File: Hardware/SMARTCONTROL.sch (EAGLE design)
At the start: 36 parts, among them IC1 ESP12-SMT, J1 ESPFLASH-1X6-2.54-SOCKET, Q2 RJU003N03, Q3 RJU003N03, Q4 RJU003N03, Q5 RJU003N03

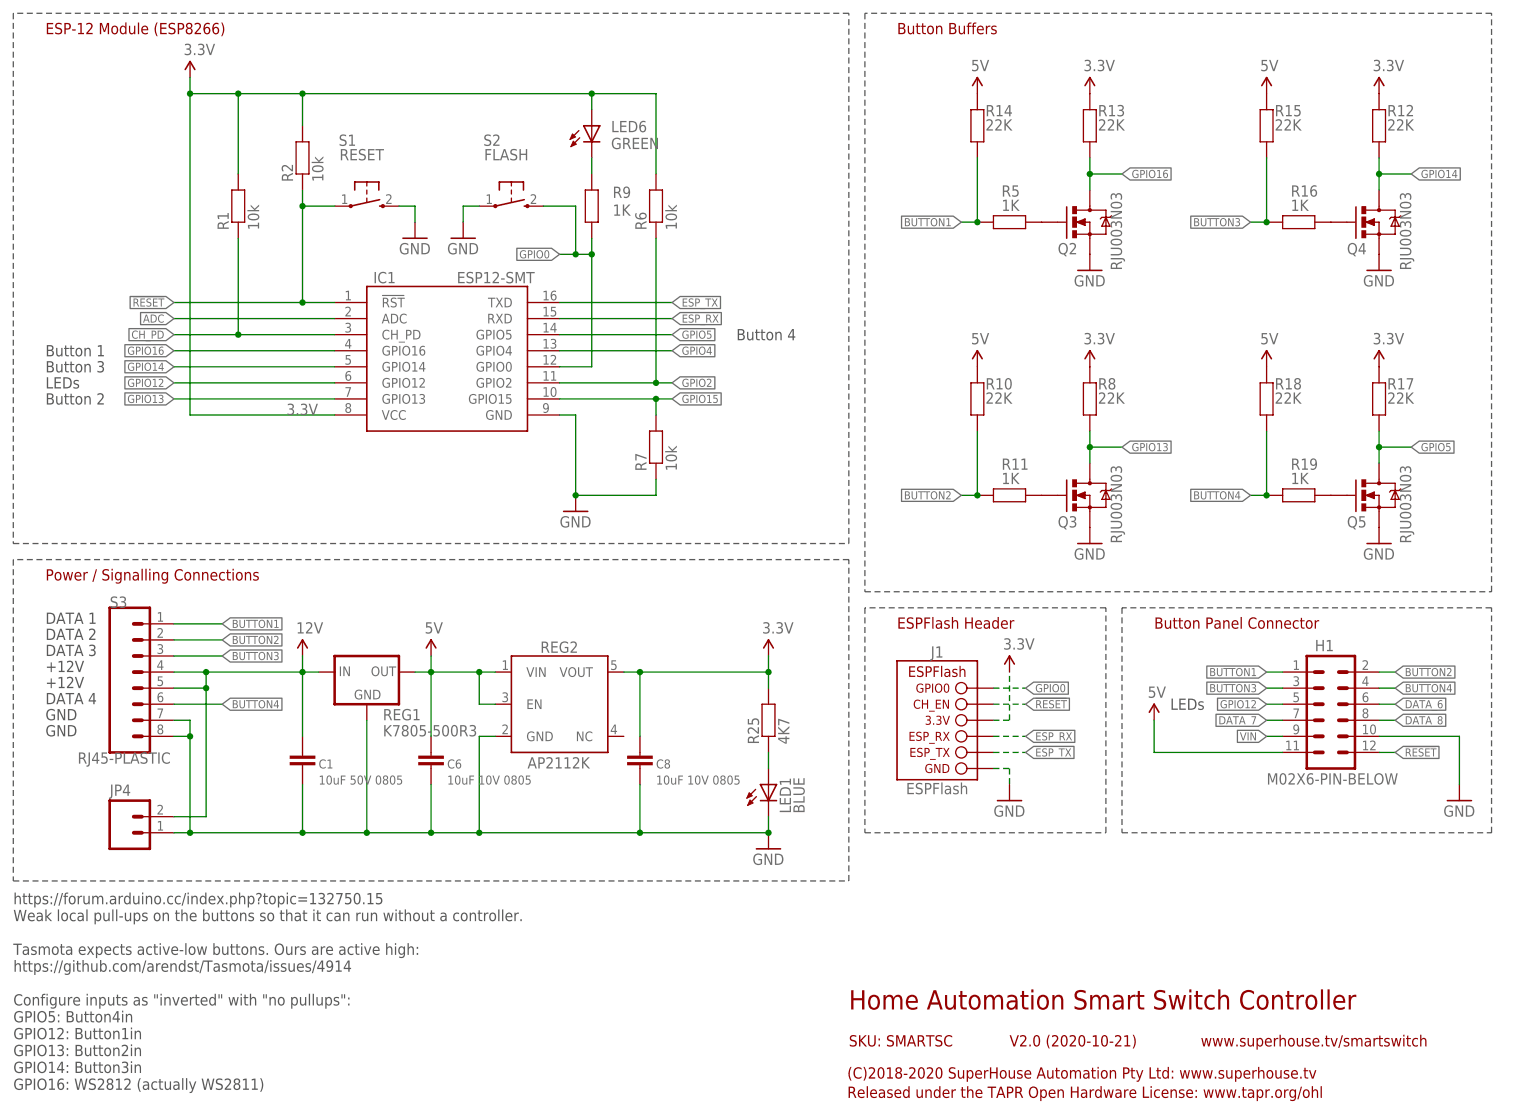
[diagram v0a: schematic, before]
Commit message: Converted switch isolation from FETs to diodes for v2.1 release.
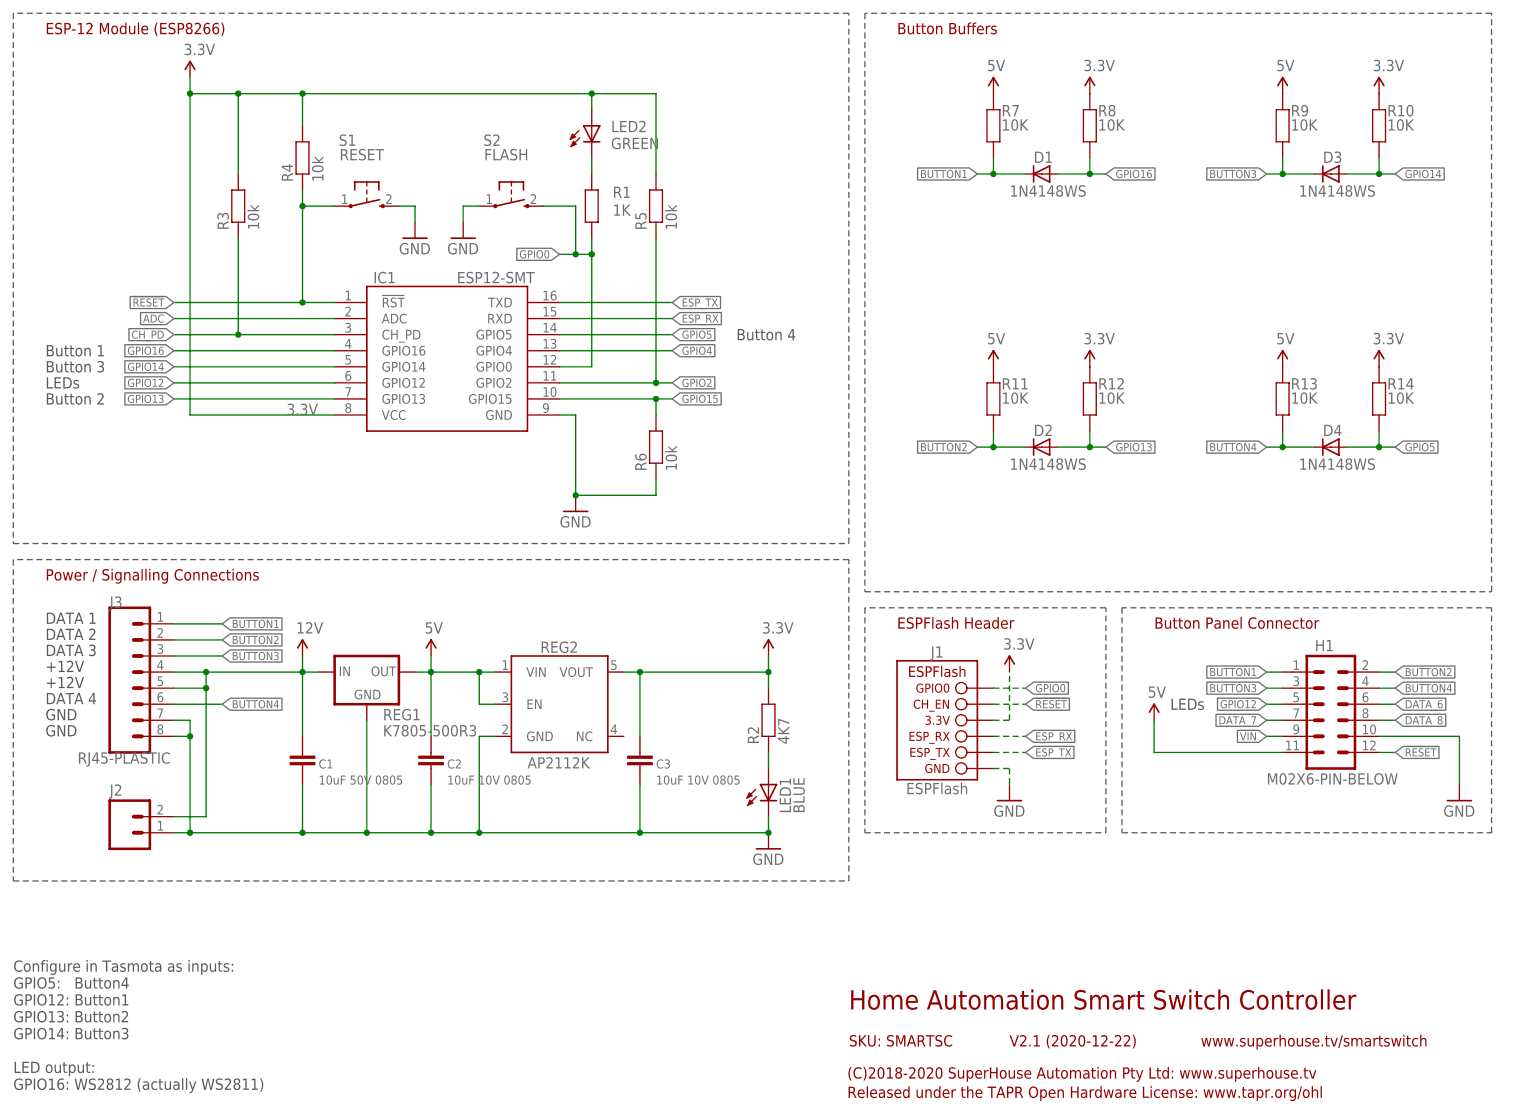
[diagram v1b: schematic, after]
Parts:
- removed Q2, Q3, Q4, Q5: RJU003N03, SuperHouse-DiscreteSemi:MOSFET-NCHANNEL-323
- removed R15, R17, R18: 22K, SuperHouse-DiscreteSemi:RESISTOR0603
- removed R16, R19: 1K, SuperHouse-DiscreteSemi:RESISTOR0603
- removed R25: 4K7, SuperHouse-DiscreteSemi:RESISTOR0603
- added D1, D2, D3, D4: 1N4148WS, SuperHouse-DiscreteSemi:DIODESOD
- added R3, R4: 10k, SuperHouse-DiscreteSemi:RESISTOR0603
- R1: value 10k -> 1K
- R10, R12, R13, R14, R8: value 22K -> 10K
- R11, R9: value 1K -> 10K
- R2: value 10k -> 4K7
- R5: value 1K -> 10k
- R7: value 10k -> 10K
- renumbered C6 to C2, C8 to C3, JP4 to J2, LED6 to LED2, S3 to J3
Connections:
- removed net N$1: Q2.G, R5.1
- removed net N$2: Q3.G, R11.1
- removed net N$3: Q4.G, R16.1
- removed net N$4: Q5.G, R19.1
- net !RESET: now also R4.1; no longer R2.1
- net 3.3V: now also R10.2, R14.2, R3.2, R4.2, R5.2; no longer R1.2, R13.2, R17.2, R25.2, R6.2
- net 5V: now also R11.2, R13.2, R7.2, R9.2; no longer R10.2, R14.2, R15.2, R18.2
- net BUTTON1: now also D1.C, R7.1; no longer R14.1, R5.2
- net BUTTON2: now also D2.C, R11.1; no longer R10.1, R11.2
- net BUTTON3: now also D3.C, R9.1; no longer R15.1, R16.2
- net BUTTON4: now also D4.C, R13.1; no longer R18.1, R19.2
- net CH_PD: now also R3.1; no longer R1.1
- net GND: now also R6.1; no longer Q2.S, Q3.S, Q4.S, Q5.S, R7.1
- net GPIO0: now also R1.2; no longer R9.2
- net GPIO13: now also D2.A, R12.1; no longer Q3.D, R8.1
- net GPIO14: now also D3.A, R10.1; no longer Q4.D, R12.1
- net GPIO15: now also R6.2; no longer R7.2
- net GPIO16: now also D1.A, R8.1; no longer Q2.D, R13.1
- net GPIO2: now also R5.1; no longer R6.1
- net GPIO5: now also D4.A, R14.1; no longer Q5.D, R17.1
- net N$23: now also R2.1; no longer R25.1
- net N$27: now also R1.1; no longer R9.1
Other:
- note added: "Configure in Tasmota as inputs: GPIO5: Button4 GPIO12: Button1 GPIO13: Button2 GPIO14: Button3 LED output: GPIO16: WS2812 (actually WS2811)"
- note added: "V2.1 (2020-12-22)"
- note removed: "V2.0 (2020-10-21)"
- note removed: "https://forum.arduino.cc/index.php?topic=132750.15 Weak local pull-ups on the buttons so that it can run without a controller. Tasmota expects active-low buttons. Ours are active high: https://github.com/arendst/Tasmota/issues/4914 Configure inputs as "inverted" with "no pullups": GPIO5: Button4in GPIO12: Button1in GPIO13: Button2in GPIO14: Button3in GPIO16: WS2812 (actually WS2811)"
- moved on the sheet: R1, R10, R11, R12, R13, R14, R2, R5, R6, R7, R8, R9
